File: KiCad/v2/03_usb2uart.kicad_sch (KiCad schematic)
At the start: 8 parts, among them IC301 CP2102N-A02-GQFN20R, J201 USB_C_Receptacle_USB2.0_16P, U201 USBLC6-2SC6

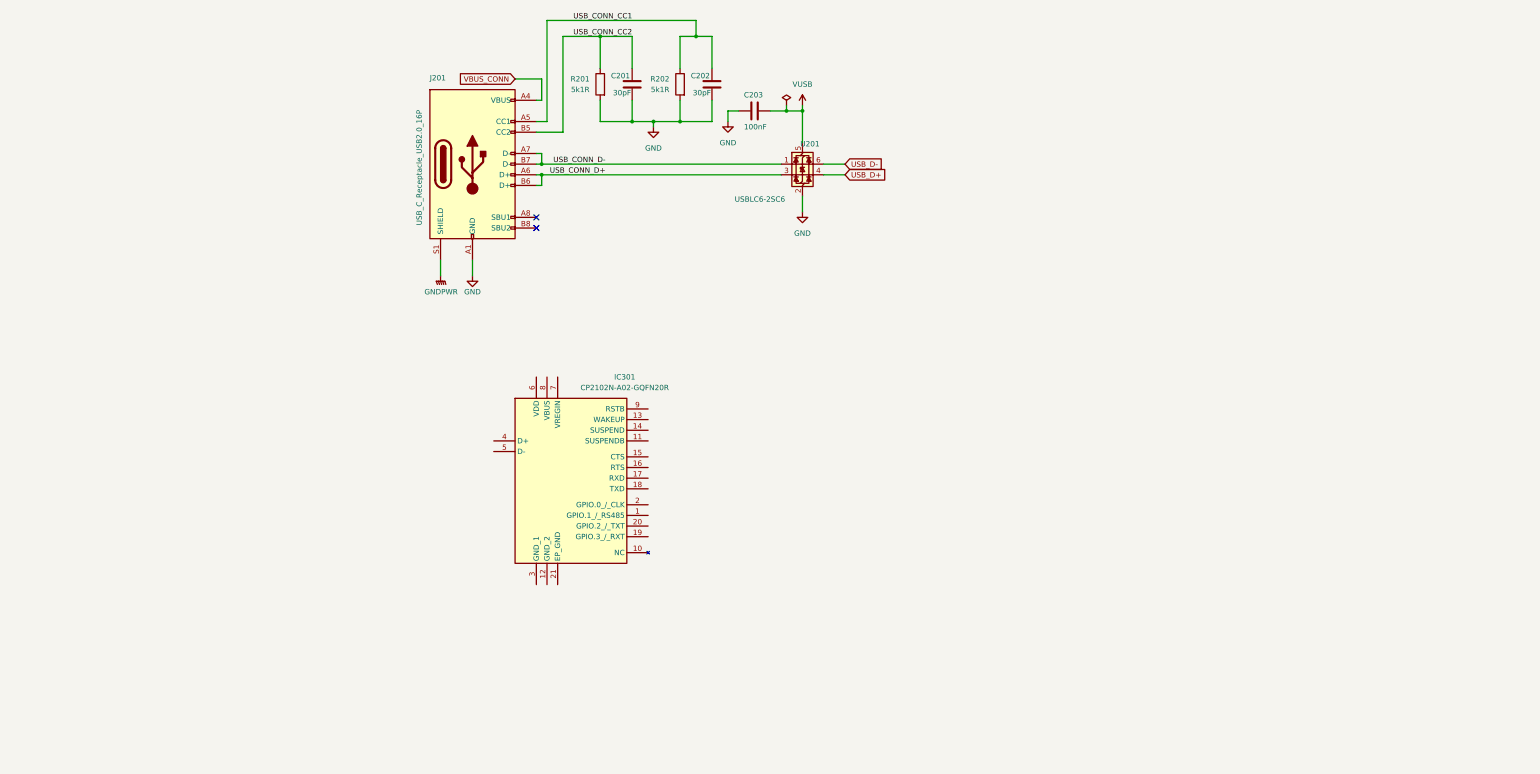
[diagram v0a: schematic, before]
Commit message: USB2UART scheme update
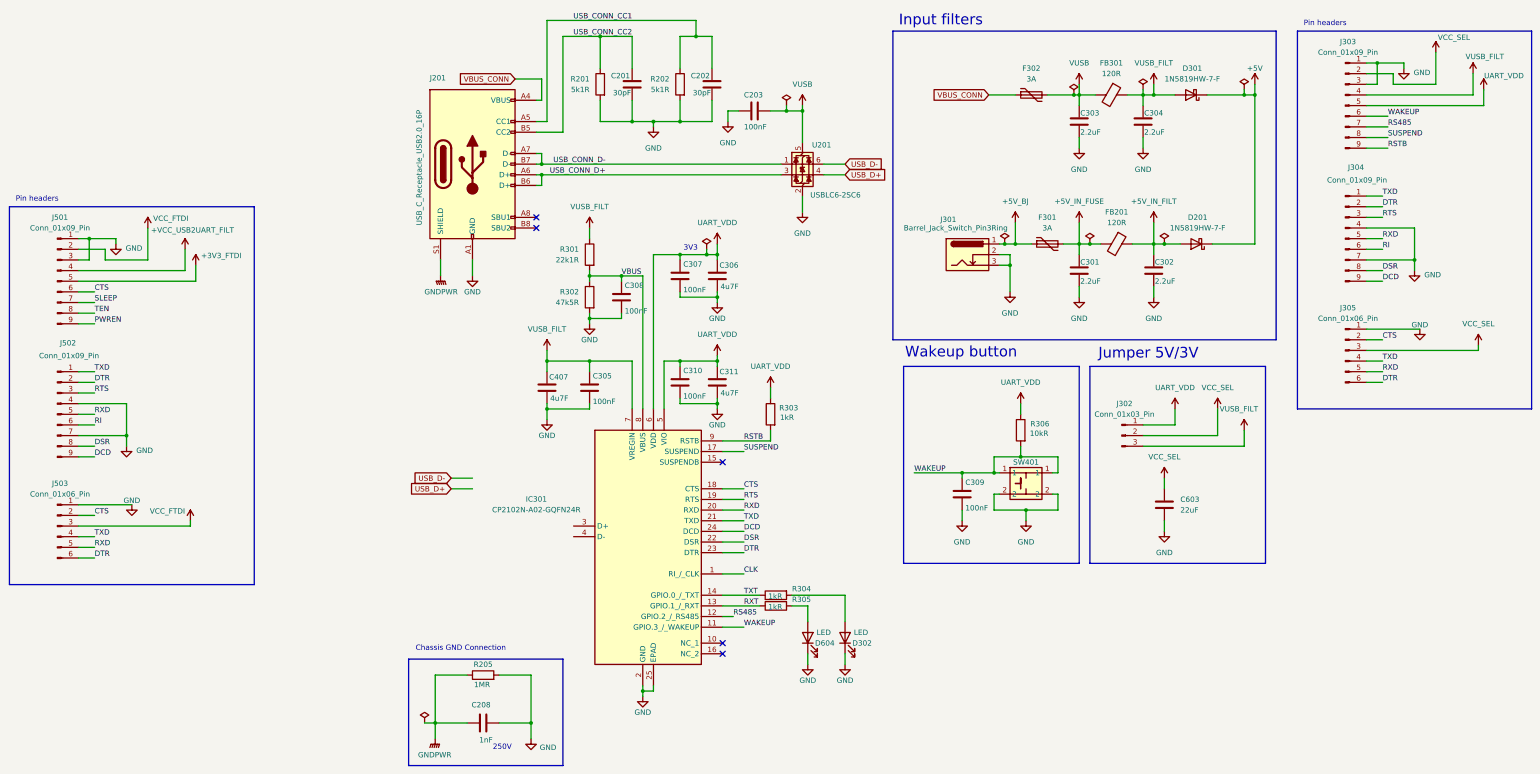
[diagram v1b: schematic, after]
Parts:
- removed IC301: CP2102N-A02-GQFN20R, psu:CP2102NA02GQFN20, symbol psu:CP2102N-A02-GQFN20R
- added C208: 1nF, Capacitor_SMD:C_0603_1608Metric, symbol Device:C
- added C301, C302, C303, C304: 2.2uF, Capacitor_SMD:C_0603_1608Metric, symbol Device:C
- added C305, C307, C308, C309, C310: 100nF, Capacitor_SMD:C_0603_1608Metric, symbol Device:C
- added C306, C311, C407: 4u7F, Capacitor_SMD:C_0805_2012Metric, symbol Device:C
- added C603: 22uF, Capacitor_SMD:C_0603_1608Metric, symbol Device:C
- added D201, D301: 1N5819HW-7-F, Diode_SMD:D_SOD-123, symbol Device:D_Schottky
- added D302, D604: LED, LED_SMD:LED_0603_1608Metric, symbol Device:LED
- added F301, F302: 3A, Fuse:Fuse_0805_2012Metric, symbol Device:Polyfuse
- added FB201, FB301: 120R, Fuse:Fuse_0603_1608Metric, symbol Device:FerriteBead
- added IC301: CP2102N-A02-GQFN24R, psu:QFN50P400X400X80-25N-D, symbol psu:CP2102N-A02-GQFN24R
- added J301: Barrel_Jack_Switch_Pin3Ring, Connector_BarrelJack:BarrelJack_GCT_DCJ200-10-A_Horizontal, symbol Connector:Barrel_Jack_Switch_Pin3Ring
- added J302: Conn_01x03_Pin, Connector_PinHeader_2.54mm:PinHeader_1x03_P2.54mm_Vertical, symbol Connector:Conn_01x03_Pin
- added J303, J304, J501, J502: Conn_01x09_Pin, Connector_PinHeader_2.54mm:PinHeader_1x09_P2.54mm_Vertical, symbol Connector:Conn_01x09_Pin
- added J305, J503: Conn_01x06_Pin, Connector_PinHeader_2.54mm:PinHeader_1x06_P2.54mm_Vertical, symbol Connector:Conn_01x06_Pin
- added R205: 1MR, Resistor_SMD:R_0805_2012Metric, symbol Device:R
- added R301: 22k1R, Resistor_SMD:R_0805_2012Metric, symbol Device:R
- added R302: 47k5R, Resistor_SMD:R_0805_2012Metric, symbol Device:R
- added R303, R304, R305: 1kR, Resistor_SMD:R_0805_2012Metric, symbol Device:R
- added R306: 10kR, Resistor_SMD:R_0805_2012Metric, symbol Device:R
- added SW401: ~, workie_talkie:SW_PUSH_6mm_H5mm, symbol workie_talkie:SW_PUSH_6mm_H5mm
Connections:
- net GND: now also C208.2, C301.2, C302.2, C303.2, C304.2, C305.2, C306.2, C307.2, C308.2, C309.2, C310.2, C311.2, C407.2, C603.2, D302.1 (K), D604.1 (K), IC301.2 (GND), IC301.25 (EPAD), J301.2, J301.3, J303.1 (Pin_1), J303.3 (Pin_3), J304.4 (Pin_4), J304.7 (Pin_7), J305.1 (Pin_1), J501.1 (Pin_1), J501.3 (Pin_3), J502.4 (Pin_4), J502.7 (Pin_7), J503.1 (Pin_1), R205.2, R302.2, SW401.2
- net GNDPWR: now also C208.1, R205.1
- net VBUS_CONN: now also F302.1
- net VUSB: now also C303.1, F302.2, FB301.2
- new net: D604.2 (A), R305.2
- new net: D302.2 (A), R304.2
- new net +3V3_FTDI: J501.5 (Pin_5)
- new net +5V: D201.1 (K), D301.1 (K)
- new net +5V_BJ: F301.1, J301.1
- new net +5V_IN_FILT: C302.1, D201.2 (A), FB201.1
- new net +5V_IN_FUSE: C301.1, F301.2, FB201.2
- new net +VCC_USB2UART_FILT: J501.4 (Pin_4)
- new net CLK: IC301.1 (RI_/_CLK)
- new net CTS: IC301.18 (CTS), J305.2 (Pin_2), J501.6 (Pin_6), J503.2 (Pin_2)
- new net DCD: IC301.24 (DCD), J304.9 (Pin_9), J502.9 (Pin_9)
- new net DSR: IC301.22 (DSR), J304.8 (Pin_8), J502.8 (Pin_8)
- new net DTR: IC301.23 (DTR), J304.2 (Pin_2), J305.6 (Pin_6), J502.2 (Pin_2), J503.6 (Pin_6)
- new net PWREN: J501.9 (Pin_9)
- new net RI: J304.6 (Pin_6), J502.6 (Pin_6)
- new net RS485: IC301.12 (GPIO.2_/_RS485), J303.7 (Pin_7)
- new net RSTB: IC301.9 (RSTB), J303.9 (Pin_9), R303.2
- new net RTS: IC301.19 (RTS), J304.3 (Pin_3), J502.3 (Pin_3)
- new net RXD: IC301.20 (RXD), J304.5 (Pin_5), J305.5 (Pin_5), J502.5 (Pin_5), J503.5 (Pin_5)
- new net RXT: IC301.13 (GPIO.1_/_RXT), R305.1
- new net SLEEP: J501.7 (Pin_7)
- new net SUSPEND: IC301.17 (SUSPEND), J303.8 (Pin_8)
- new net TEN: J501.8 (Pin_8)
- new net TXD: IC301.21 (TXD), J304.1 (Pin_1), J305.4 (Pin_4), J502.1 (Pin_1), J503.4 (Pin_4)
- new net TXT: IC301.14 (GPIO.0_/_TXT), R304.1
- new net UART_VDD: C306.1, C307.1, C310.1, C311.1, IC301.5 (VIO), IC301.6 (VDD), J302.1 (Pin_1), J303.5 (Pin_5), R303.1, R306.1
- new net VBUS: C308.1, IC301.8 (VBUS), R301.2, R302.1
- new net VCC_FTDI: J501.2 (Pin_2), J503.3 (Pin_3)
- new net VCC_SEL: C603.1, J302.2 (Pin_2), J303.2 (Pin_2), J305.3 (Pin_3)
- new net VUSB_FILT: C304.1, C305.1, C407.1, D301.2 (A), FB301.1, IC301.7 (VREGIN), J302.3 (Pin_3), J303.4 (Pin_4), R301.1
- new net WAKEUP: C309.1, IC301.11 (GPIO.3_/_WAKEUP), J303.6 (Pin_6), R306.2, SW401.1
- no-connect marks 2 -> 5
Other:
- note added: "250V"
- note added: "3V3"
- note added: "Chassis GND Connection"
- note added: "Input filters"
- note added: "Jumper 5V/3V"
- note added: "Pin headers"
- note added: "Wakeup button"

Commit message: scheme for voltage regulators
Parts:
- removed C301, C302, C303, C304: 2.2uF, Capacitor_SMD:C_0603_1608Metric, symbol Device:C
- removed D201, D301: 1N5819HW-7-F, Diode_SMD:D_SOD-123, symbol Device:D_Schottky
- removed F301, F302: 3A, Fuse:Fuse_0805_2012Metric, symbol Device:Polyfuse
- removed FB201, FB301: 120R, Fuse:Fuse_0603_1608Metric, symbol Device:FerriteBead
- removed J301: Barrel_Jack_Switch_Pin3Ring, Connector_BarrelJack:BarrelJack_GCT_DCJ200-10-A_Horizontal, symbol Connector:Barrel_Jack_Switch_Pin3Ring
- removed J501, J502: Conn_01x09_Pin, Connector_PinHeader_2.54mm:PinHeader_1x09_P2.54mm_Vertical, symbol Connector:Conn_01x09_Pin
- removed J503: Conn_01x06_Pin, Connector_PinHeader_2.54mm:PinHeader_1x06_P2.54mm_Vertical, symbol Connector:Conn_01x06_Pin
- added D301: LED, LED_SMD:LED_0603_1608Metric, symbol Device:LED
- added D304: 1N5819HW-7-F, Diode_SMD:D_SOD-123, symbol Device:D_Schottky
- added R306: 1kR, Resistor_SMD:R_0402_1005Metric, symbol Device:R
- R301, R302, R303: footprint Resistor_SMD:R_0805_2012Metric -> Resistor_SMD:R_0402_1005Metric
- R304: renamed from R201; footprint Resistor_SMD:R_0805_2012Metric -> Resistor_SMD:R_0402_1005Metric
- R305: renamed from R202; footprint Resistor_SMD:R_0805_2012Metric -> Resistor_SMD:R_0402_1005Metric
- R307: renamed from R304; footprint Resistor_SMD:R_0805_2012Metric -> Resistor_SMD:R_0402_1005Metric
- R308: renamed from R305; footprint Resistor_SMD:R_0805_2012Metric -> Resistor_SMD:R_0402_1005Metric
- R309: renamed from R306; footprint Resistor_SMD:R_0805_2012Metric -> Resistor_SMD:R_0402_1005Metric
- R310: renamed from R205; footprint Resistor_SMD:R_0805_2012Metric -> Resistor_SMD:R_0402_1005Metric
- renumbered C307 to C301, C306 to C302, C308 to C303, C310 to C304, C311 to C305, C407 to C306, C305 to C307, C201 to C308, C202 to C309, C203 to C310, C309 to C311, C603 to C312, C208 to C313, D604 to D302, D302 to D303, J303 to J301, J304 to J302, J305 to J303, J201 to J304, J302 to J305, SW401 to SW301, U201 to U301
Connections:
- net GND: now also D301.1 (K)
- net SUSPEND: now also R306.1
- net USB_D+: now also IC301.3 (D+)
- net USB_D-: now also IC301.4 (D-)
- net VCC_SEL: now also D304.1 (K); no longer J305.2 (Pin_2)
- new net: D304.2 (A), J305.2 (Pin_2)
- new net: D301.2 (A), R306.2
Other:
- note added: "[3] USB 2 UART"
- note removed: "Input filters"
- moved on the sheet: C301, C302, C303, C304, C305, C306, C307, C308, C309, C310, C311, C312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

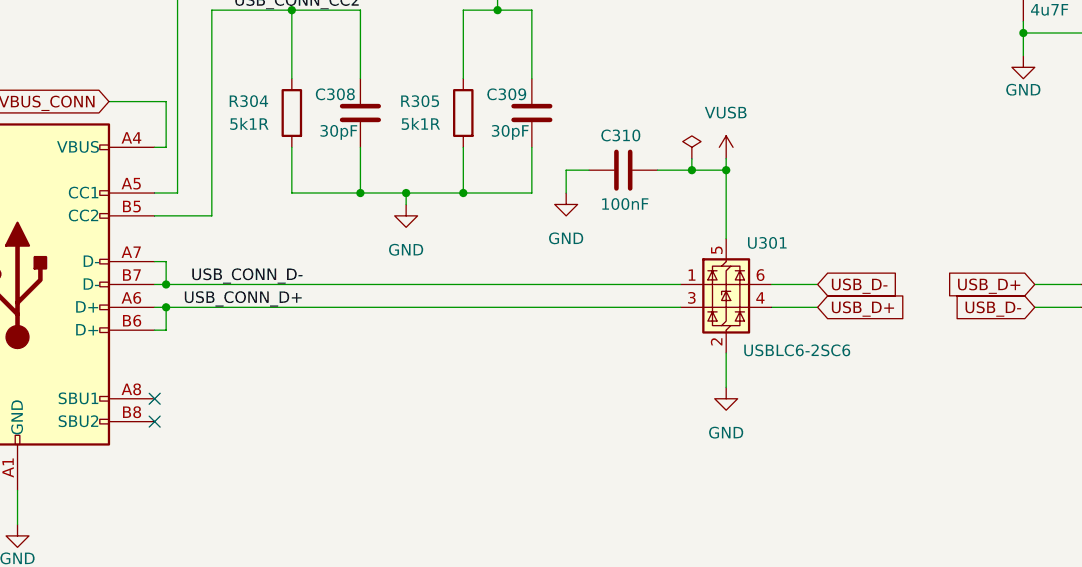
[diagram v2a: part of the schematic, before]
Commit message: Update USB connection scheme
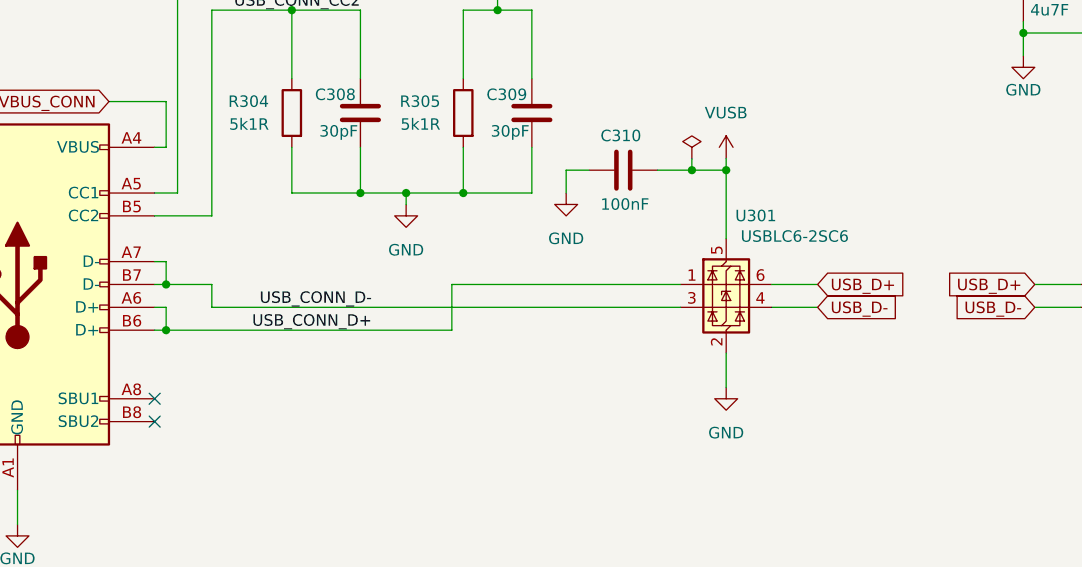
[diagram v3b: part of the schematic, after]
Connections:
- net USB_CONN_D+: now also U301.1 (I/O1); no longer U301.3 (I/O2)
- net USB_CONN_D-: now also U301.3 (I/O2); no longer U301.1 (I/O1)
- net USB_D+: now also U301.6 (I/O1); no longer U301.4 (I/O2)
- net USB_D-: now also U301.4 (I/O2); no longer U301.6 (I/O1)
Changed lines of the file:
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@@
 	)
 	(junction
-		(at 48.26 99.06)
-		(diameter 0)
-		(color 0 0 0 0)
-	)
-	(junction
 		(at 110.49 86.36)
 		(diameter 0)
@@
 	)
 	(junction
-		(at 48.26 101.6)
-		(diameter 0)
-		(color 0 0 0 0)
-	)
-	(junction
 		(at 181.61 34.29)
 		(diameter 0)
@@
 	)
 	(junction
+		(at 48.26 99.06)
+		(diameter 0)
+		(color 0 0 0 0)
+	)
+	(junction
 		(at 184.15 59.69)
 		(diameter 0)
@@
 	)
 	(junction
+		(at 48.26 104.14)
+		(diameter 0)
+		(color 0 0 0 0)
+	)
+	(junction
 		(at 85.09 68.58)
 		(diameter 0)
@@
 	(wire
 		(pts
-			(xy 48.26 101.6) (xy 105.41 101.6)
+			(xy 53.34 99.06) (xy 48.26 99.06)
 		)
 		(stroke
@@
 	(wire
 		(pts
+			(xy 115.57 101.6) (xy 120.65 101.6)
+		)
+		(stroke
+			(width 0)
+			(type default)
+		)
+	)
+	(wire
+		(pts
 			(xy 81.28 83.82) (xy 81.28 88.9)
 		)
@@
 	(wire
 		(pts
+			(xy 53.34 101.6) (xy 53.34 99.06)
+		)
+		(stroke
+			(width 0)
+			(type default)
+		)
+	)
+	(wire
+		(pts
 			(xy 41.91 78.74) (xy 48.26 78.74)
 		)
@@
 	(wire
 		(pts
+			(xy 105.41 99.06) (xy 80.01 99.06)
+		)
+		(stroke
+			(width 0)
+			(type default)
+		)
+	)
+	(wire
+		(pts
+			(xy 80.01 99.06) (xy 80.01 104.14)
+		)
+		(stroke
+			(width 0)
+			(type default)
+		)
+	)
+	(wire
+		(pts
 			(xy 53.34 91.44) (xy 53.34 68.58)
 		)
@@
 	(wire
 		(pts
+			(xy 115.57 99.06) (xy 120.65 99.06)
+		)
+		(stroke
+			(width 0)
+			(type default)
+		)
+	)
+	(wire
+		(pts
 			(xy 139.7 181.61) (xy 139.7 177.8)
 		)
@@
 	(wire
 		(pts
-			(xy 115.57 99.06) (xy 120.65 99.06)
-		)
-		(stroke
-			(width 0)
-			(type default)
-		)
-	)
-	(wire
-		(pts
 			(xy 184.15 43.18) (xy 184.15 44.45)
 		)
@@
 	(wire
 		(pts
-			(xy 115.57 101.6) (xy 120.65 101.6)
-		)
-		(stroke
-			(width 0)
-			(type default)
-		)
-	)
-	(wire
-		(pts
 			(xy 24.13 121.92) (xy 24.13 125.73)
 		)
@@
 	(wire
 		(pts
-			(xy 130.81 168.91) (xy 139.7 168.91)
+			(xy 48.26 104.14) (xy 80.01 104.14)
 		)
 		(stroke
@@
 	(wire
 		(pts
-			(xy 185.42 105.41) (xy 190.5 105.41)
+			(xy 130.81 168.91) (xy 139.7 168.91)
 		)
 		(stroke
@@
 	(wire
 		(pts
-			(xy 242.57 91.44) (xy 246.38 91.44)
+			(xy 185.42 105.41) (xy 190.5 105.41)
 		)
 		(stroke
@@
 	(wire
 		(pts
-			(xy 48.26 99.06) (xy 105.41 99.06)
+			(xy 242.57 91.44) (xy 246.38 91.44)
 		)
 		(stroke
@@
 	(wire
 		(pts
+			(xy 53.34 101.6) (xy 105.41 101.6)
+		)
+		(stroke
+			(width 0)
+			(type default)
+		)
+	)
+	(wire
+		(pts
 			(xy 158.75 48.26) (xy 158.75 49.53)
 		)
@@
 	)
 	(label "USB_CONN_D+"
-		(at 63.5 101.6 180)
+		(at 71.12 104.14 180)
 		(effects
 			(font
@@
 	)
 	(label "USB_CONN_D-"
-		(at 63.5 99.06 180)
+		(at 71.12 101.6 180)
 		(effects
 			(font
@@
 	(global_label "USB_D-"
 		(shape input)
-		(at 120.65 99.06 0)
+		(at 120.65 101.6 0)
 		(fields_autoplaced yes)
 		(effects
@@
 		)
 		(property "Intersheetrefs" "${INTERSHEET_REFS}"
-			(at 131.2552 99.06 0)
+			(at 131.2552 101.6 0)
 			(effects
 				(font
@@
 	(global_label "USB_D+"
 		(shape input)
-		(at 120.65 101.6 0)
+		(at 120.65 99.06 0)
 		(fields_autoplaced yes)
 		(effects
@@
 		)
 		(property "Intersheetrefs" "${INTERSHEET_REFS}"
-			(at 131.2552 101.6 0)
+			(at 131.2552 99.06 0)
 			(effects
 				(font
@@
 		(dnp no)
 		(property "Reference" "U301"
-			(at 115.062 94.488 0)
+			(at 113.792 91.44 0)
 			(effects
 				(font
@@
 		)
 		(property "Value" "USBLC6-2SC6"
-			(at 118.364 106.426 0)
+			(at 118.11 93.726 0)
 			(effects
 				(font

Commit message: Scheme updates
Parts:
- removed SW301: ~, workie_talkie:SW_PUSH_6mm_H5mm, symbol workie_talkie:SW_PUSH_6mm_H5mm
- added SW301: ~, psu:SW_PUSH_6mm_H5mm, symbol psu:SW_PUSH_6mm_H5mm
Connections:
- net GND: now also SW301.2
- net WAKEUP: now also SW301.1
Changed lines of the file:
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@@
+	)
+	(symbol
+		(lib_id "psu:SW_PUSH_6mm_H5mm")
+		(at 132.08 173.99 0)
+		(unit 1)
+		(exclude_from_sim no)
+		(in_bom yes)
+		(on_board yes)
+		(dnp no)
+		(property "Reference" "SW301"
+			(at 132.08 170.18 0)
+			(effects
+				(font
+					(size 1.27 1.27)
+				)
+			)
+		)
+		(property "Value" "~"
+			(at 131.572 179.578 0)
+			(effects
+				(font
+					(size 1.27 1.27)
+				)
+			)
+		)
+		(property "Footprint" "psu:SW_PUSH_6mm_H5mm"
+			(at 132.08 180.848 0)
+			(effects
+				(font
+					(size 1.27 1.27)
+				)
+				(hide yes)
+			)
+		)
+		(property "Datasheet" ""
+			(at 132.08 173.99 0)
+			(effects
+				(font
+					(size 1.27 1.27)
+				)
+				(hide yes)
+			)
+		)
+		(property "Description" ""
+			(at 132.08 173.99 0)
+			(effects
+				(font
+					(size 1.27 1.27)
+				)
+				(hide yes)
+			)
+		)
+		(pin "2"
+		)
+		(pin "1"
+		)
+		(pin "1"
+		)
+		(pin "2"
+		)
+		(instances
+			(project "solderless_breadboard_psu"
+				(path "/6d24fac5-4a4b-49b5-80a0-bc8a42e41061/b185057a-45c8-4512-8009-8ada1a85e4bb"
+					(reference "SW301")
+					(unit 1)
+				)
+			)
+		)
 	)
 	(symbol
@@
 					(unit 1)
 				)
-			)
-		)
-	)
-	(symbol
-		(lib_id "workie_talkie:SW_PUSH_6mm_H5mm")
-		(at 132.08 173.99 0)
-		(unit 1)
-		(exclude_from_sim no)
-		(in_bom yes)
-		(on_board yes)
-		(dnp no)
-		(property "Reference" "SW301"
-			(at 132.08 170.18 0)
-			(effects
-				(font
-					(size 1.27 1.27)
-				)
-			)
-		)
-		(property "Value" "~"
-			(at 132.08 168.91 0)
-			(effects
-				(font
-					(size 1.27 1.27)
-				)
-			)
-		)
-		(property "Footprint" "workie_talkie:SW_PUSH_6mm_H5mm"
-			(at 132.842 180.594 0)
-			(effects
-				(font
-					(size 1.27 1.27)
-				)
-				(hide yes)
-			)
-		)
-		(property "Datasheet" ""
-			(at 132.08 173.99 0)
-			(effects
-				(font
-					(size 1.27 1.27)
-				)
-				(hide yes)
-			)
-		)
-		(property "Description" ""
-			(at 132.08 173.99 0)
-			(effects
-				(font
-					(size 1.27 1.27)
-				)
-				(hide yes)
-			)
-		)
-		(property "LCSC Part Number" "C29781314"
-			(at 132.08 173.99 0)
-			(effects
-				(font
-					(size 1.27 1.27)
-				)
-				(hide yes)
-			)
-		)
-		(property "Manufacturer" "SM Switch"
-			(at 132.08 173.99 0)
-			(effects
-				(font
-					(size 1.27 1.27)
-				)
-				(hide yes)
-			)
-		)
-		(property "Manufacturer Part Number" "SMG-01-H080A1"
-			(at 132.08 173.99 0)
-			(effects
-				(font
-					(size 1.27 1.27)
-				)
-				(hide yes)
-			)
-		)
-		(pin "1"
-		)
-		(pin "2"
-		)
-		(pin "1"
-		)
-		(pin "2"
-		)
-		(instances
-			(project "solderless_breadboard_psu"
-				(path "/6d24fac5-4a4b-49b5-80a0-bc8a42e41061/b185057a-45c8-4512-8009-8ada1a85e4bb"
-					(reference "SW301")
-					(unit 1)
-				)
